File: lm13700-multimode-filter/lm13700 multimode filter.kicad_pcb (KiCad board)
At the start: 2 copper layers, 65 x 95 mm, 53 parts, among them J1 Power In, J2 Audio In, J3 CV-in, J4 High Pass, J5 Band Pass, J6 Low pass, Q1 2N3906, Q2 2N3906, U1 TL074, U2 TL072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

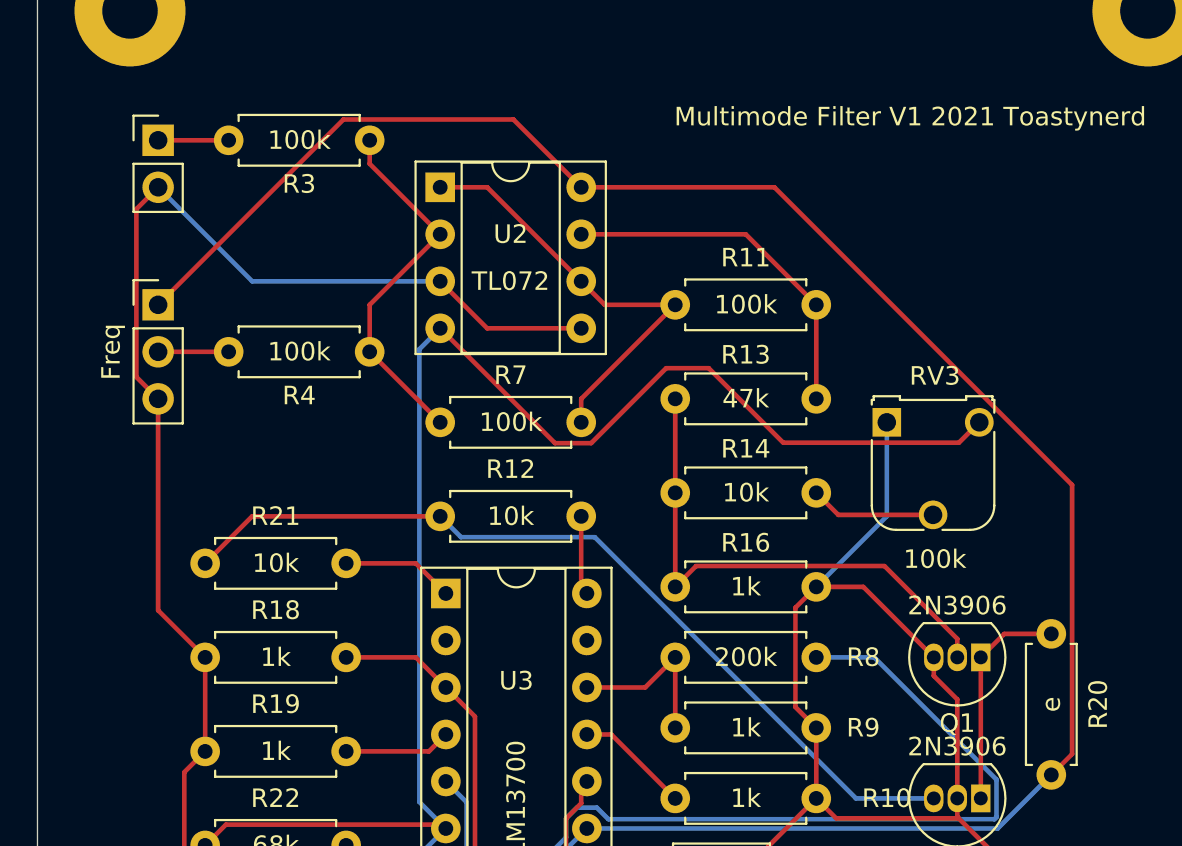
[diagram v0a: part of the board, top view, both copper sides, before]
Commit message: 555 stencils and lm13700 stuff
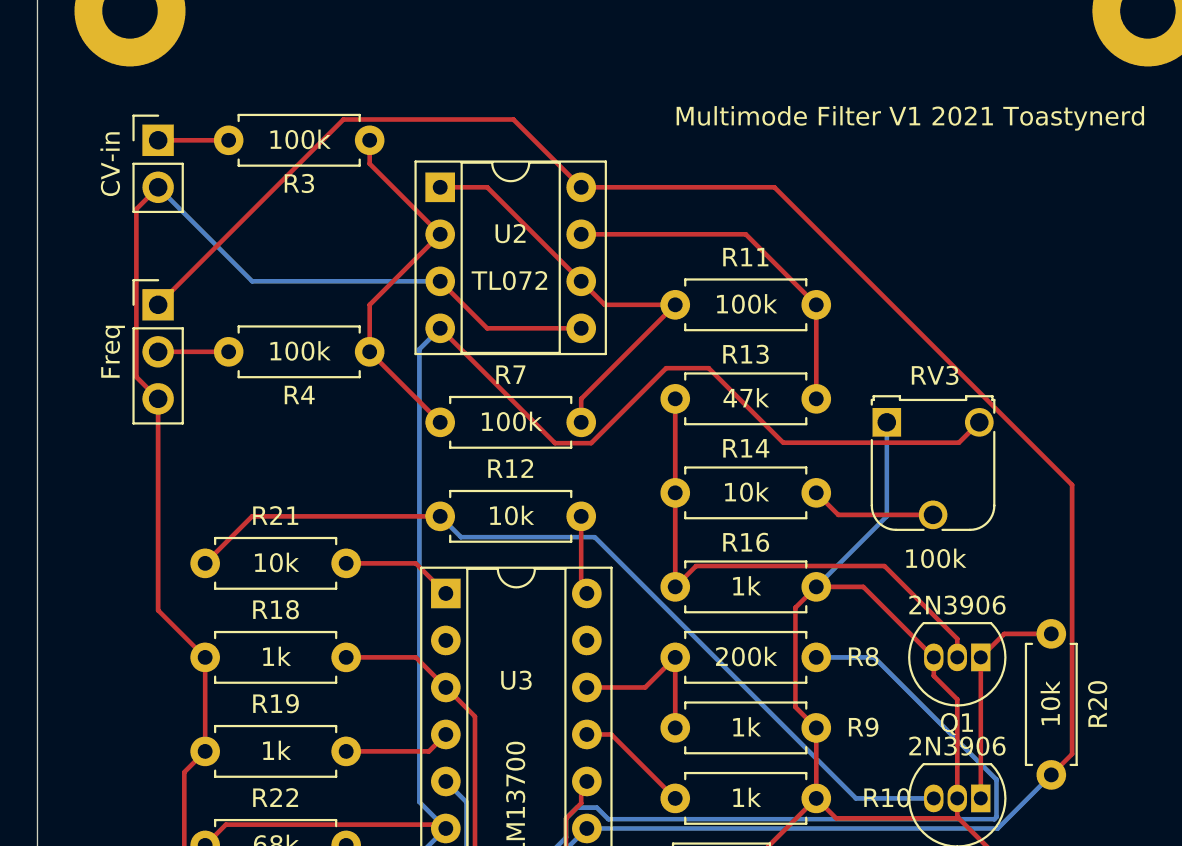
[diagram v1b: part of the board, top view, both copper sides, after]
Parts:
- R20: value e -> 10k

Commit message: add: panels
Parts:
- added R29: 100k, Resistor_THT:R_Axial_DIN0207_L6.3mm_D2.5mm_P7.62mm_Horizontal, F.Cu at (119.2, 43.2)
- RV1: value Freq -> a100k
- RV2: value Reso -> 1M
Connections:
- R7 pad 1: Net-(R11-Pad2) -> Net-(R29-Pad2)
- U2 pad 1: Net-(R11-Pad2) -> Net-(R29-Pad2)
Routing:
- net Net-(R29-Pad2): track 0.00 -> 22.3 mm
- net Net-(R11-Pad2): track 23.8 -> 17.9 mm
